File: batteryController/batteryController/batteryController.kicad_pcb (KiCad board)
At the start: 4 copper layers, 42.5 x 28 mm, 15 parts, among them J1 Conn_01x02_Male, J2 Screw_Terminal_01x02, J3 Conn_01x04_Male, J4 Conn_01x04_Male, J5 Conn_01x04_Male, J6 USB_A, U1 ATtiny13V-10P, U2 L7806CV, U3 L78L05_TO92

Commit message: remade basically the entire thing
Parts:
- removed D1: LED, LED_THT:LED_D3.0mm
- removed J1: Conn_01x02_Male, Connector_PinHeader_2.54mm:PinHeader_1x02_P2.54mm_Vertical
- removed J3, J4, J5: Conn_01x04_Male, Connector_PinHeader_2.54mm:PinHeader_1x04_P2.54mm_Vertical
- removed R1: 220, Resistor_THT:R_Axial_DIN0207_L6.3mm_D2.5mm_P7.62mm_Horizontal
- added J7: Conn_02x08_Counter_Clockwise, Connector_PinHeader_2.54mm:PinHeader_2x08_P2.54mm_Vertical, F.Cu at (195.1, 115.8)
- R2, R4: value R -> 2k; footprint Resistor_THT:R_Axial_DIN0207_L6.3mm_D2.5mm_P7.62mm_Horizontal -> Resistor_SMD:R_0603_1608Metric; moved to B.Cu
- R3, R5: value R -> 680; footprint Resistor_THT:R_Axial_DIN0207_L6.3mm_D2.5mm_P7.62mm_Horizontal -> Resistor_SMD:R_0603_1608Metric; moved to B.Cu
- U2: moved to B.Cu
- U3: value L78L05_TO92 -> L78L05_SOT89; footprint Package_TO_SOT_THT:TO-92_Inline -> Package_TO_SOT_SMD:SOT-89-3; moved to B.Cu
- moved R2 87.3 mm to (202.5, 106.0), turned to 90 degrees
- moved U3 87.1 mm to (207.0, 105.0), turned to 180 degrees
- moved R3 82.8 mm to (200.5, 106.0), turned to 90 degrees
- moved U1 82.8 mm to (198.2, 108.8), turned to 90 degrees
- moved R4 77.0 mm to (197.0, 104.0)
- moved R5 76.5 mm to (199.0, 104.0)
- moved J2 62.2 mm to (212.0, 108.1)
- moved J6 50.2 mm to (183.8, 122.0)
- moved U2 31.6 mm to (176.3, 108.5)
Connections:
- net Net-(J6-Pad2) renamed /D-
- net Net-(J6-Pad3) renamed /D+
- U1 pad 5: unconnected-(U1-Pad5) -> /controll pin
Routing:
- net /controll pin: track 0.00 -> 24.2 mm
- net /VBUS: track 42.7 -> 66.0 mm
- net /6V: track 19.6 -> 40.2 mm
- net /5V: track 30.4 -> 40.3 mm, vias 0 -> 2
- net Net-(R3-Pad1): track 8.66 -> 2.07 mm
- net /D+: track 20.1 -> 25.3 mm, vias 0 -> 1
- net Net-(D1-Pad1): track 4.43 -> 0.00 mm
- net Net-(R4-Pad1): track 8.67 -> 4.57 mm
- net Net-(R2-Pad1): track 6.03 -> 2.30 mm
- net Net-(J7-Pad14): track 0.00 -> 2.96 mm
- net Net-(J7-Pad6): track 0.00 -> 2.54 mm
- net Net-(J7-Pad5): track 0.00 -> 2.54 mm
- net Net-(J5-Pad3): track 2.54 -> 0.00 mm
- net Net-(J4-Pad3): track 2.54 -> 0.00 mm
- net Net-(J3-Pad3): track 2.54 -> 0.00 mm
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- added copper zone on B.Cu, net /GND
- removed copper zone on In1.Cu, net /GND
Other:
- board size 42.5 x 28 mm -> 44 x 18 mm
- copper layers 4 -> 2
- board text added: "G"
- board text removed: "GND"

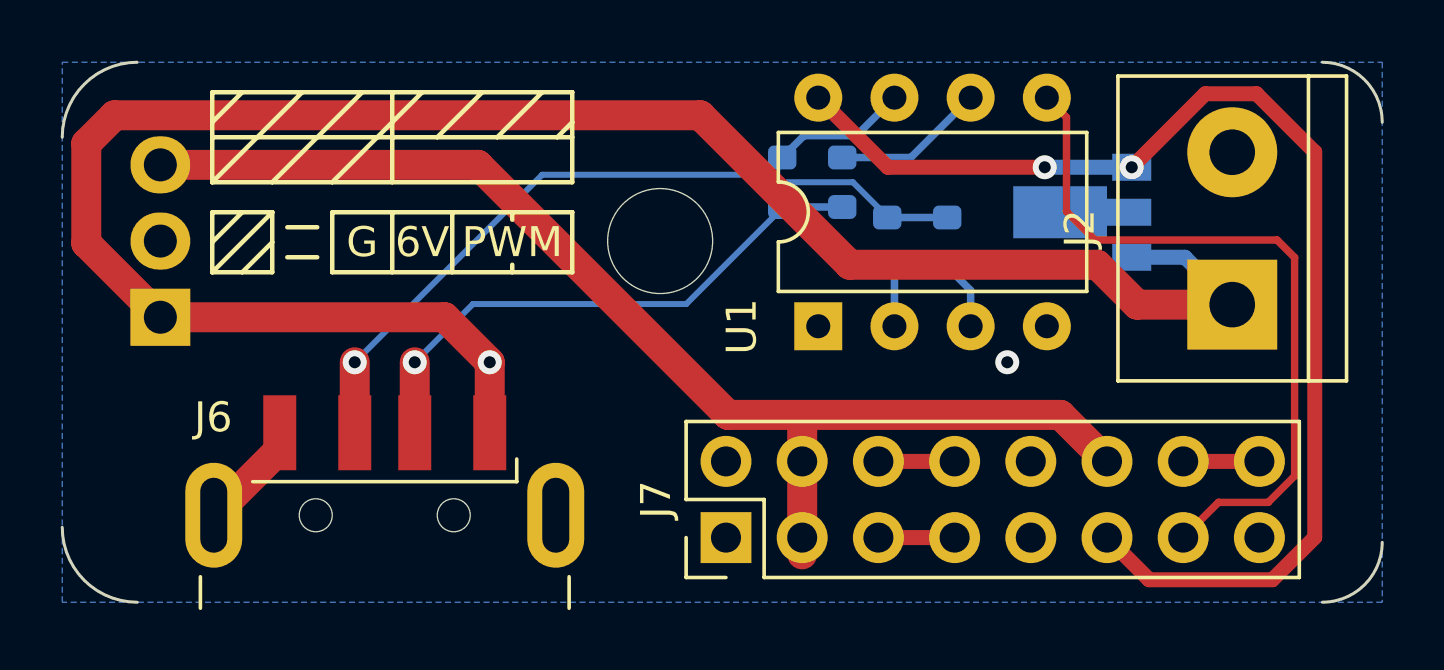
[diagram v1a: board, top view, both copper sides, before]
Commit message: fixed DRC warnings
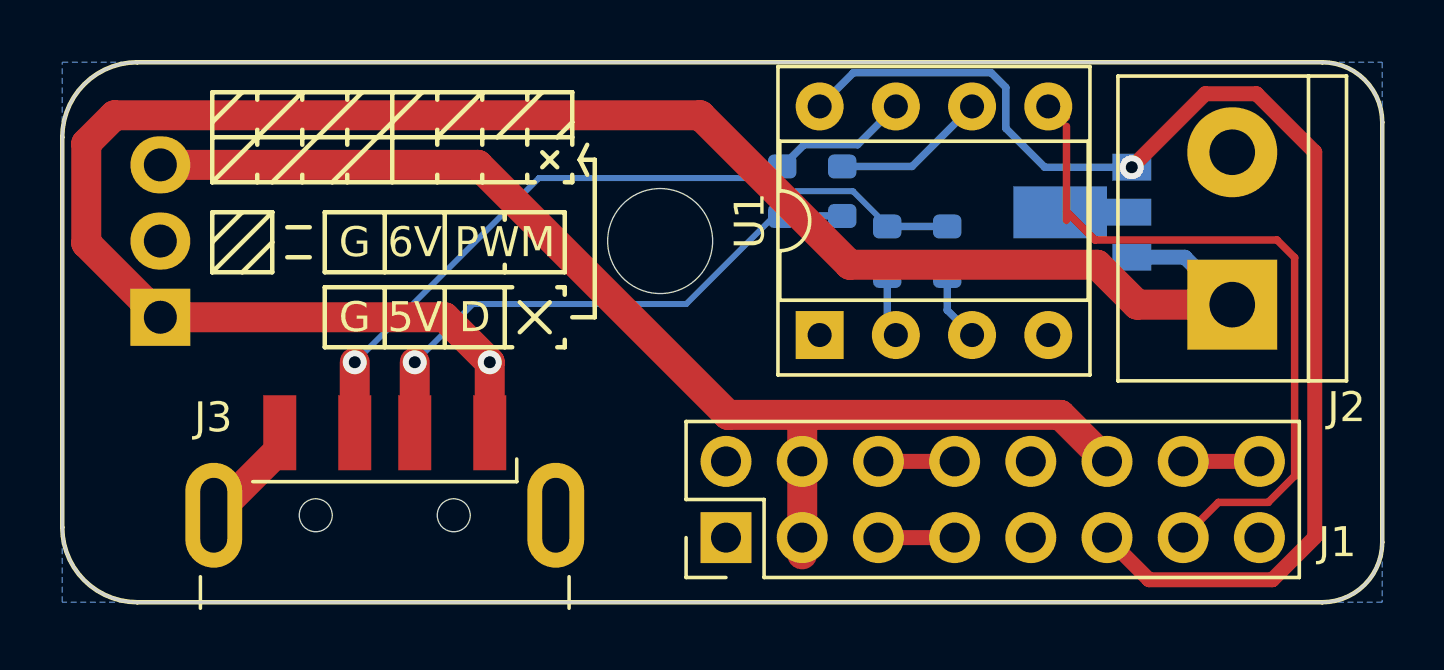
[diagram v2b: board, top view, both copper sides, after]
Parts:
- U1: value ATtiny13V-10P -> ATtiny45V-10P; footprint Package_DIP:DIP-8_W7.62mm -> Package_DIP:DIP-8_W7.62mm_Socket
- moved R1 0.30 mm to (202.5, 106.3)
- moved R2 0.30 mm to (200.5, 106.3)
- moved R3 0.30 mm to (197.0, 104.3)
- moved R4 0.30 mm to (199.0, 104.3)
- moved U1 0.30 mm to (198.2, 109.1)
- renumbered J7 to J1, J6 to J3, R2 to R1, R3 to R2, R4 to R3, R5 to R4
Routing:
- net /5V: track 40.3 -> 41.8 mm, vias 2 -> 1
- net /GND: vias 1 -> 0
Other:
- board text added: "5V"
- board text added: "D"

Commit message: added radius marker
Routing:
- net /6V: track 40.2 -> 39.7 mm
- net /VBUS: vias 1 -> 0
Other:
- board text added: "3mm"
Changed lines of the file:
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@@
   (gr_arc (start 173 102.5) (mid 173.732233 100.732233) (end 175.5 100) (layer "B.SilkS") (width 0.15))
   (gr_line (start 217 102) (end 217 116) (layer "B.SilkS") (width 0.15))
+  (gr_line (start 175.5 118) (end 175.75 117.5) (layer "B.SilkS") (width 0.15))
   (gr_line (start 215 118) (end 175.5 118) (layer "B.SilkS") (width 0.15))
+  (gr_line (start 175.5 115.5) (end 175.25 116) (layer "B.SilkS") (width 0.15))
   (gr_arc (start 175.5 118) (mid 173.732233 117.267767) (end 173 115.5) (layer "B.SilkS") (width 0.15))
   (gr_arc (start 217 116) (mid 216.414214 117.414214) (end 215 118) (layer "B.SilkS") (width 0.15))
   (gr_arc (start 215 100) (mid 216.414214 100.585786) (end 217 102) (layer "B.SilkS") (width 0.15))
+  (gr_line (start 175.5 115.5) (end 175.75 116) (layer "B.SilkS") (width 0.15))
   (gr_line (start 175.5 100) (end 215 100) (layer "B.SilkS") (width 0.15))
+  (gr_line (start 175.5 118) (end 175.25 117.5) (layer "B.SilkS") (width 0.15))
+  (gr_line (start 175.25 117.5) (end 175.5 118) (layer "B.SilkS") (width 0.15))
   (gr_line (start 173 115.5) (end 173 102.5) (layer "B.SilkS") (width 0.15))
+  (gr_line (start 175.5 115.5) (end 175.5 118) (layer "B.SilkS") (width 0.15))
   (gr_line (start 181.75 107) (end 189.75 107) (layer "F.SilkS") (width 0.15))
   (gr_line (start 185.75 107.5) (end 185.75 109.5) (layer "F.SilkS") (width 0.15))
@@
   (gr_line (start 175.5 100) (end 215 100) (layer "Edge.Cuts") (width 0.1))
   (gr_arc (start 175.5 118) (mid 173.732233 117.267767) (end 173 115.5) (layer "Edge.Cuts") (width 0.1))
+  (gr_text "3mm" (at 175.25 114.5) (layer "B.SilkS")
+    (effects (font (size 1 1) (thickness 0.15)) (justify mirror))
+  )
   (gr_text "G" (at 182.75 108.5) (layer "F.SilkS")
     (effects (font (size 1 1) (thickness 0.15)))
@@
   (segment (start 176.27 108.5) (end 173.80048 106.03048) (width 1) (layer "F.Cu") (net 2))
   (segment (start 207.5 106.75) (end 208.83 108.08) (width 1) (layer "F.Cu") (net 2))
-  (via (at 187.25 110) (size 0.8) (drill 0.4) (layers "F.Cu" "B.Cu") (free) (net 2))
   (segment (start 210.42 106.5) (end 212 108.08) (width 0.5) (layer "B.Cu") (net 2))
   (segment (start 208.65 106.5) (end 210.42 106.5) (width 0.5) (layer "B.Cu") (net 2))
-  (segment (start 206.474511 104.974511) (end 207.42548 105.92548) (width 0.25) (layer "F.Cu") (net 3))
-  (segment (start 207.42548 105.92548) (end 213.494502 105.92548) (width 0.25) (layer "F.Cu") (net 3))
-  (segment (start 213.494502 105.92548) (end 214.079511 106.510489) (width 0.25) (layer "F.Cu") (net 3))
-  (segment (start 206.474511 102.133511) (end 206.474511 105.273511) (width 0.25) (layer "F.Cu") (net 3))
-  (segment (start 214.079511 106.510489) (end 214.079511 113.791499) (width 0.25) (layer "F.Cu") (net 3))
-  (segment (start 213.200521 114.670489) (end 211.539511 114.670489) (width 0.25) (layer "F.Cu") (net 3))
-  (segment (start 214.079511 113.791499) (end 213.200521 114.670489) (width 0.25) (layer "F.Cu") (net 3))
-  (segment (start 205.82 101.18) (end 206.474511 101.834511) (width 0.25) (layer "F.Cu") (net 3))
-  (segment (start 211.539511 114.670489) (end 210.365 115.845) (width 0.25) (layer "F.Cu") (net 3))
+  (segment (start 211.539511 114.670489) (end 213.200521 114.670489) (width 0.25) (layer "F.Cu") (net 3))
+  (segment (start 205.867 104.367) (end 205.867 101.473) (width 0.25) (layer "F.Cu") (net 3))
+  (segment (start 210.365 115.845) (end 211.539511 114.670489) (width 0.25) (layer "F.Cu") (net 3))
+  (segment (start 207.42548 105.92548) (end 205.867 104.367) (width 0.25) (layer "F.Cu") (net 3))
+  (segment (start 213.200521 114.670489) (end 214.079511 113.791499) (width 0.25) (layer "F.Cu") (net 3))
+  (segment (start 214.079511 106.510489) (end 213.494502 105.92548) (width 0.25) (layer "F.Cu") (net 3))
+  (segment (start 214.079511 113.791499) (end 214.079511 106.510489) (width 0.25) (layer "F.Cu") (net 3))
+  (segment (start 213.494502 105.92548) (end 207.42548 105.92548) (width 0.25) (layer "F.Cu") (net 3))
   (segment (start 180.25 112.9) (end 178.05 115.1) (width 1) (layer "F.Cu") (net 4))
   (segment (start 180.25 112.35) (end 180.25 112.9) (width 1) (layer "F.Cu") (net 4))
   (segment (start 186.855142 103.42) (end 195.190631 111.755489) (width 1) (layer "F.Cu") (net 5))
   (segment (start 206.275489 111.755489) (end 207.825 113.305) (width 1) (layer "F.Cu") (net 5))
-  (segment (start 197.665 115.845) (end 197.665 116.404022) (width 1) (layer "F.Cu") (net 5))
   (segment (start 176.27 103.42) (end 186.855142 103.42) (width 1) (layer "F.Cu") (net 5))
   (segment (start 197.665 113.305) (end 197.665 115.845) (width 1) (layer "F.Cu") (net 5))
@@
   (segment (start 184.75 110) (end 186.690479 108.059521) (width 0.2) (layer "B.Cu") (net 6))
   (segment (start 186.690479 108.059521) (end 193.799651 108.059521) (width 0.2) (layer "B.Cu") (net 6))
-  (segment (start 197 105.158172) (end 197 105.124) (width 0.2) (layer "B.Cu") (net 6))
   (segment (start 193.799651 108.059521) (end 197 104.859172) (width 0.2) (layer "B.Cu") (net 6))
   (segment (start 197 105.124) (end 199 105.124) (width 0.25) (layer "B.Cu") (net 6))
@@
   (segment (start 196.643573 104.299) (end 199.356427 104.299) (width 0.2) (layer "B.Cu") (net 7))
   (segment (start 196.643573 104.299) (end 196.205052 103.860479) (width 0.2) (layer "B.Cu") (net 7))
-  (segment (start 200.74 107.364) (end 200.5 107.124) (width 0.25) (layer "B.Cu") (net 8))
   (segment (start 200.5 107.124) (end 200.5 108.806) (width 0.25) (layer "B.Cu") (net 8))
   (segment (start 200.5 108.806) (end 200.787 109.093) (width 0.25) (layer "B.Cu") (net 8))
@@
   (segment (start 202.745 113.305) (end 200.205 113.305) (width 0.5) (layer "F.Cu") (net 12))
   (segment (start 212.905 113.305) (end 210.365 113.305) (width 0.5) (layer "F.Cu") (net 13))
-  (segment (start 210.79 113.305) (end 210.365 113.305) (width 0.5) (layer "B.Cu") (net 13))
   (segment (start 202.5 108.266) (end 203.327 109.093) (width 0.25) (layer "B.Cu") (net 15))
   (segment (start 202.5 107.124) (end 202.5 108.266) (width 0.25) (layer "B.Cu") (net 15))

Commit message: remade it again...
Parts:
- added G***: LOGO, personal-icons:ABB-gym-logo-4mm, B.Cu at (213.0, 114.5)
- R1, R2, R3, R4: footprint Resistor_SMD:R_0603_1608Metric -> Resistor_SMD:R_0402_1005Metric; moved to F.Cu
- U2, U3: moved to F.Cu
- moved U3 10.9 mm to (212.6, 114.4), turned to 90 degrees
- moved R1 7.47 mm to (195.1, 106.9), turned to -90 degrees
- moved U2 5.94 mm to (174.8, 102.8), turned to -90 degrees
- moved J1 4.88 mm to (190.2, 116.0)
- moved R2 4.44 mm to (196.1, 106.9), turned to -90 degrees
- moved R4 4.00 mm to (195.1, 103.7), turned to 90 degrees
- moved J3 2.50 mm to (181.2, 122.0)
- moved R3 1.09 mm to (196.1, 103.7), turned to 90 degrees
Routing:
- net Net-(R1-Pad1): track 2.31 -> 9.89 mm
- net /5V: track 41.8 -> 35.2 mm
- net /D+: track 25.3 -> 19.6 mm, vias 1 -> 2
- net /VBUS: track 66.0 -> 60.7 mm, vias 0 -> 1
- net /controll pin: track 23.8 -> 18.6 mm
- net Net-(R4-Pad1): track 5.16 -> 9.90 mm
- net /6V: track 39.7 -> 35.5 mm
- net Net-(R2-Pad1): track 2.09 -> 6.21 mm
- net /D-: track 18.7 -> 21.3 mm, vias 1 -> 2
- net Net-(R3-Pad1): track 4.62 -> 5.81 mm
- net /GND: vias 0 -> 1
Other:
- board text added: "3x"
- board text added: "Designed by Algot"
